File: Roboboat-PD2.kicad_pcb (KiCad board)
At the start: 2 copper layers, 78 x 60.7 mm, 52 parts, among them J1 14.4V, J10 Motor, J11 Motor, J12 Motor, J13 Motor, J14 Motor, J15 Motor, J16 Motor, J17 GND TP, J18 PGOOD TP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

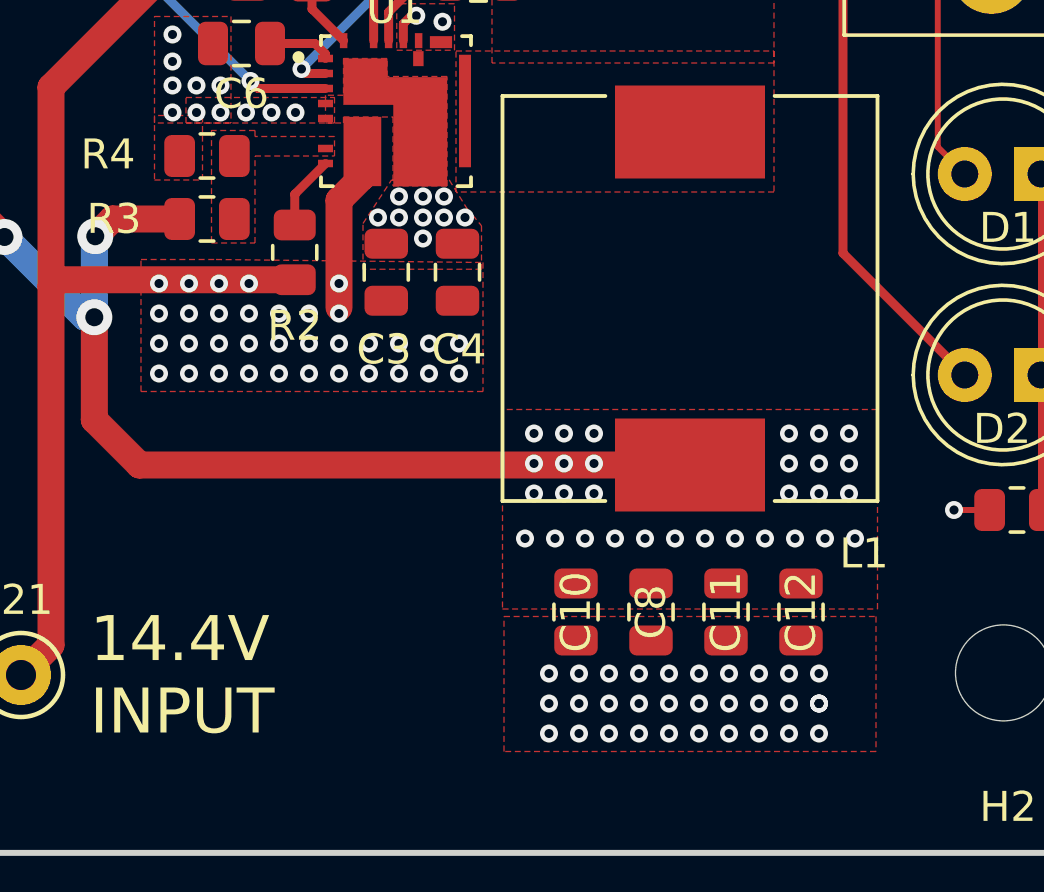
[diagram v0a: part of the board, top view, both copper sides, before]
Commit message: use less thermal vias
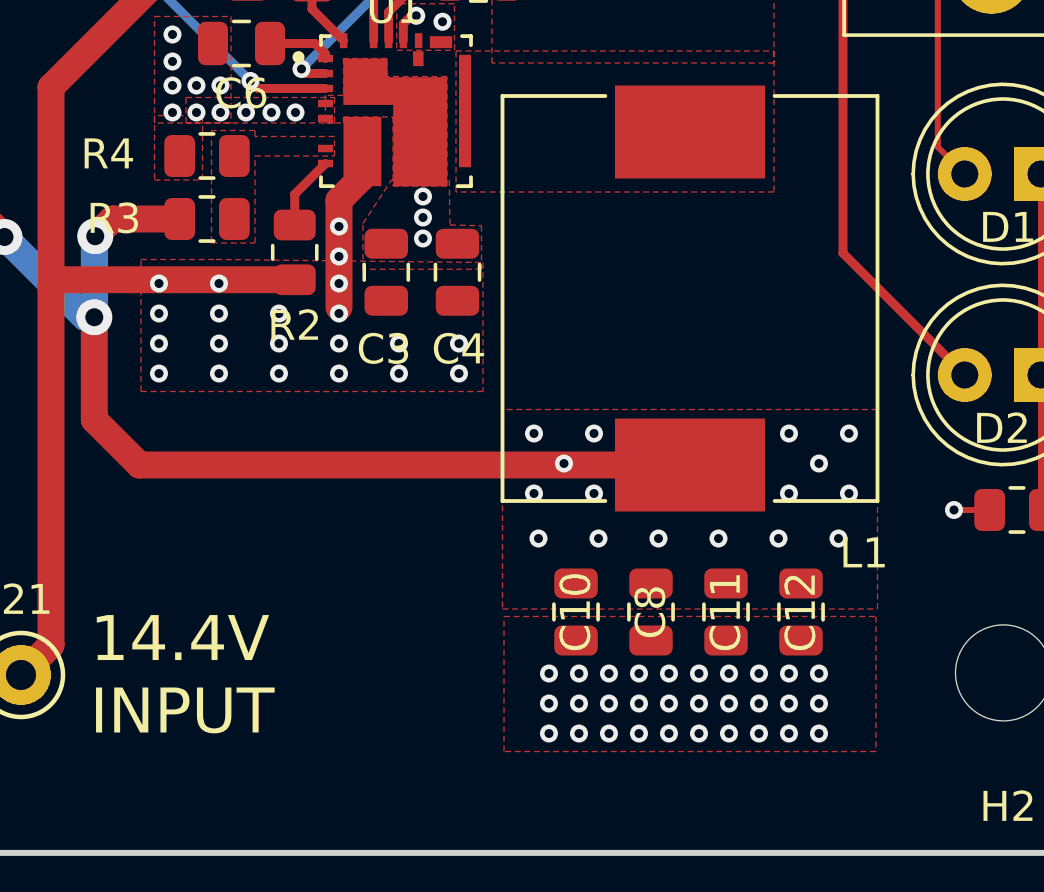
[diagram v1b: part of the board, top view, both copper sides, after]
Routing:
- net GND: vias 75 -> 68
- net +14.4V: vias 34 -> 21
- net +12V: vias 33 -> 19

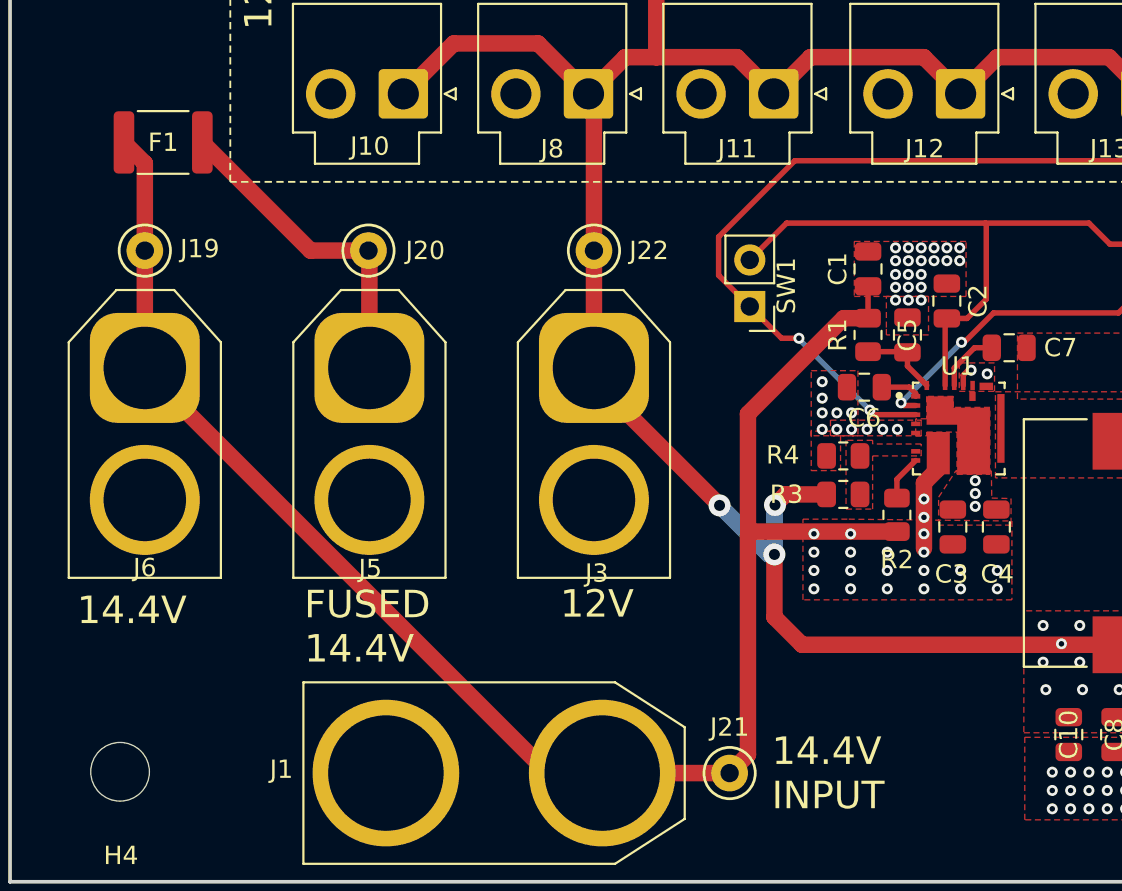
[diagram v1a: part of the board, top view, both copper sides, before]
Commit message: move fuse
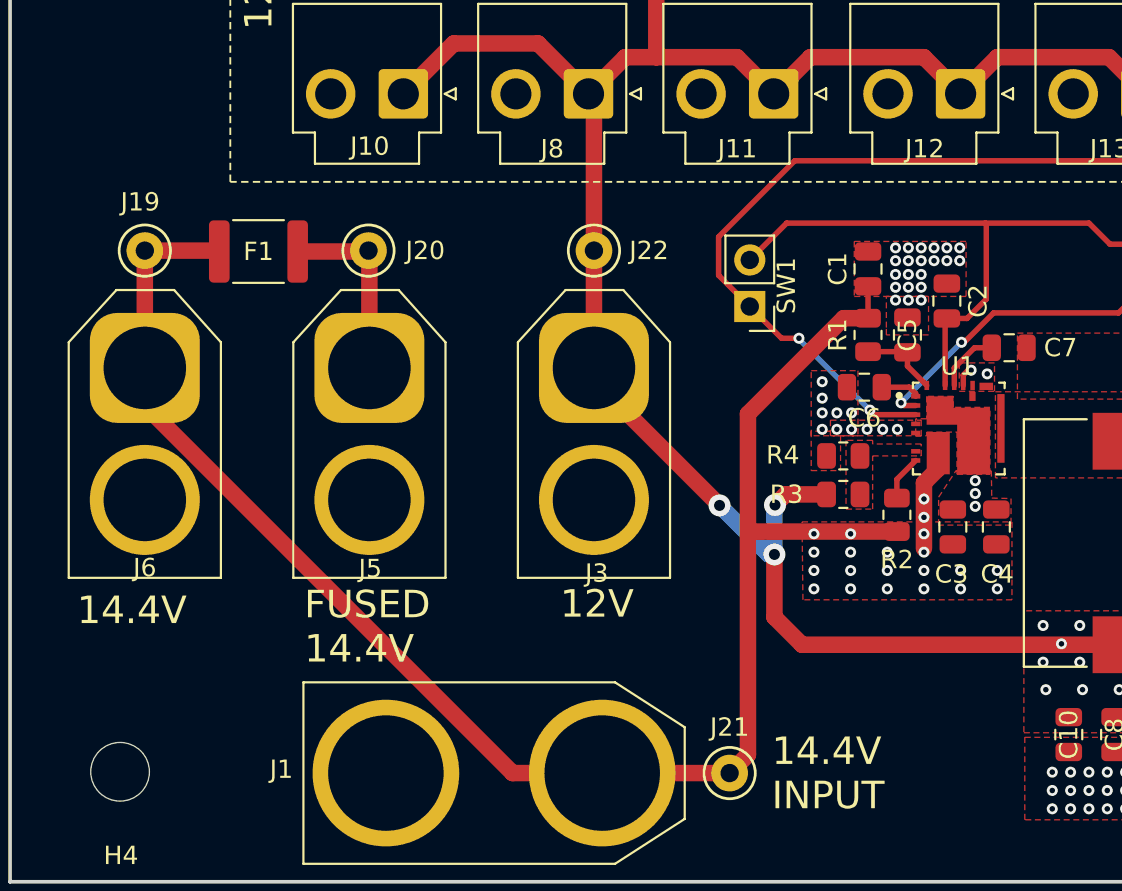
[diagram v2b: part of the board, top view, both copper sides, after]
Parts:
- moved F1 7.90 mm to (108.2, 94.6)
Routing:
- net /14.4_F: track 17.9 -> 10.2 mm
- net +14.4V: track 94.7 -> 96.6 mm
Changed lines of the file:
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@@
 		(tags "Through Hole Mount Test Points")
 		(property "Reference" "J19"
-			(at 3 -0.1 0)
+			(at -0.25 -2.65 0)
 			(layer "F.SilkS")
 			(effects
@@
 	(footprint "Fuse:Fuse_1812_4532Metric"
 		(layer "F.Cu")
-		(at 103 88.65 180)
+		(at 108.2 94.6 180)
 		(descr "Fuse SMD 1812 (4532 Metric), square (rectangular) end terminal, IPC_7351 nominal, (Body size source: https://www.nikhef.nl/pub/departments/mt/projects/detectorR_D/dtddice/ERJ2G.pdf), generated with kicad-footprint-generator")
 		(tags "fuse")
@@
 	)
 	(segment
-		(start 102 89.7875)
-		(end 100.8625 88.65)
+		(start 122.06188 123.05)
+		(end 126.95 123.05)
 		(width 0.9)
 		(layer "F.Cu")
@@
 	)
 	(segment
+		(start 102 102.98812)
+		(end 122.06188 123.05)
+		(width 0.9)
+		(layer "F.Cu")
+		(net 8)
+	)
+	(segment
 		(start 133.9 123.05)
 		(end 134.9 122.05)
@@
 	)
 	(segment
+		(start 102 94.55)
+		(end 106.0125 94.55)
+		(width 0.9)
+		(layer "F.Cu")
+		(net 8)
+	)
+	(segment
 		(start 145.28 106.445)
 		(end 145.28 105.6)
@@
 	)
 	(segment
-		(start 102 101.06188)
-		(end 123.98812 123.05)
+		(start 106.0125 94.55)
+		(end 106.0625 94.6)
 		(width 0.9)
 		(layer "F.Cu")
@@
 	)
 	(segment
-		(start 102 94.55)
-		(end 102 89.7875)
+		(start 102 100.95)
+		(end 102 102.98812)
 		(width 0.9)
 		(layer "F.Cu")
@@
 	)
 	(segment
-		(start 111.0375 94.55)
-		(end 105.1375 88.65)
+		(start 114.15 94.6)
+		(end 114.2 94.55)
 		(width 0.9)
 		(layer "F.Cu")
@@
 	)
 	(segment
-		(start 114.2 94.55)
-		(end 111.0375 94.55)
+		(start 110.3375 94.6)
+		(end 114.15 94.6)
 		(width 0.9)
 		(layer "F.Cu")
@@
 		(polygon
 			(pts
-				(xy 149.3 109.3) (xy 149.3 113.6) (xy 137.9 113.6) (xy 137.9 109.2) (xy 140.4 109.2)
+				(xy 149.3 109.35) (xy 149.3 113.6) (xy 137.9 113.6) (xy 137.85 109.35) (xy 140.4 109.35)
 			)
 		)

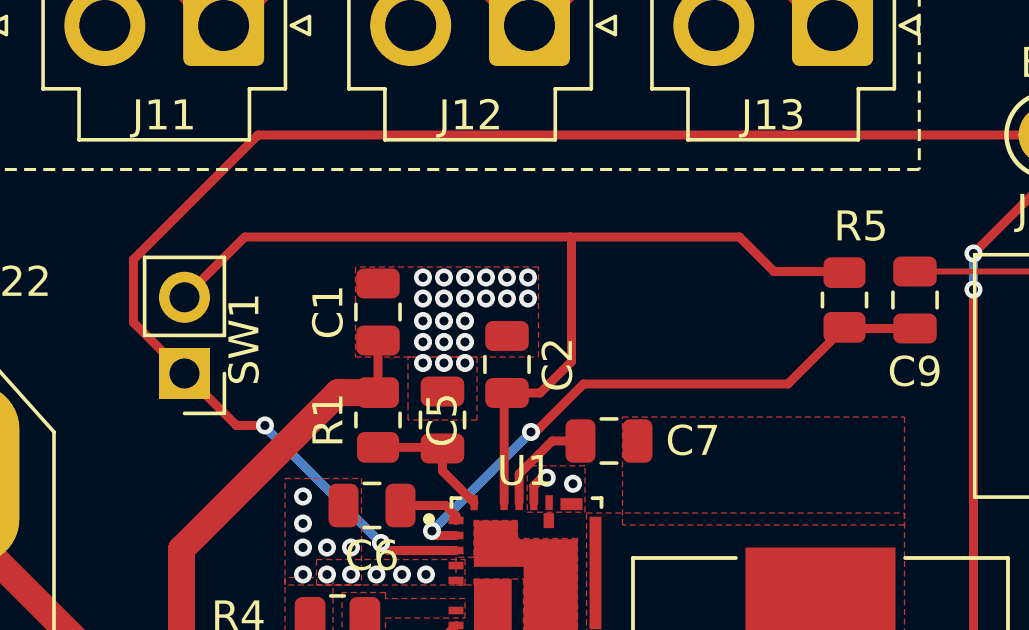
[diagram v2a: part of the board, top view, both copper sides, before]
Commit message: adjust VCC traces
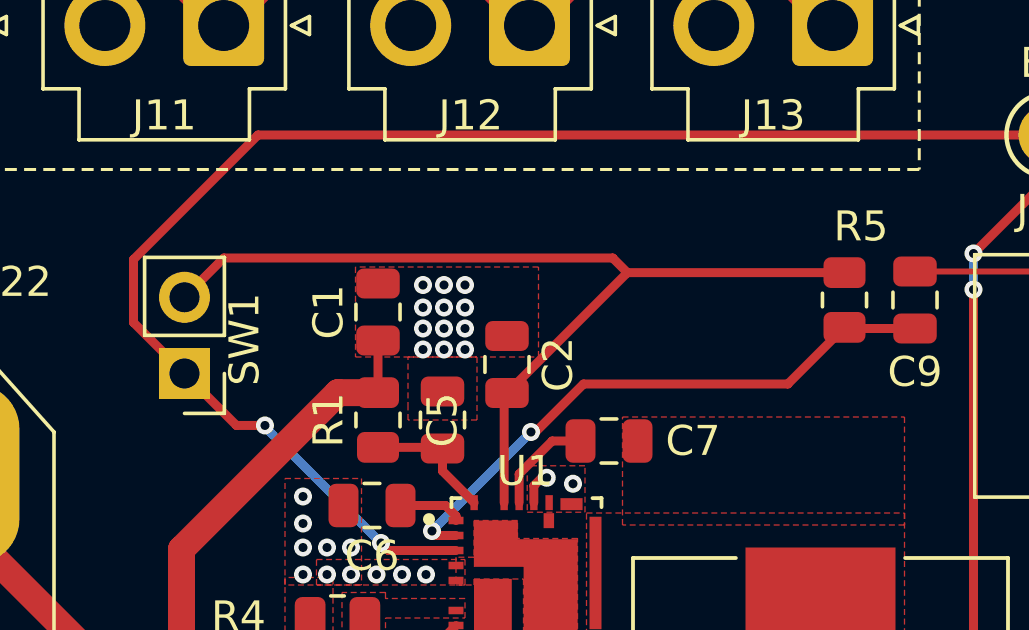
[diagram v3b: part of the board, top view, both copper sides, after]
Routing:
- net /VCC: track 33.6 -> 32.0 mm
- net GND: vias 68 -> 59
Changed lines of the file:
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@@
-	)
-	(via
-		(at 145.75 95.1)
-		(size 0.6)
-		(drill 0.3)
-		(layers "F.Cu" "B.Cu")
-		(free yes)
-		(net 1)
 	)
 	(via
@@
 	)
 	(via
-		(at 142.95 95.1)
-		(size 0.6)
-		(drill 0.3)
-		(layers "F.Cu" "B.Cu")
-		(free yes)
-		(net 1)
-	)
-	(via
-		(at 143.65 95.1)
-		(size 0.6)
-		(drill 0.3)
-		(layers "F.Cu" "B.Cu")
-		(free yes)
-		(net 1)
-	)
-	(via
-		(at 146.45 95.1)
+		(at 142.95 94.65)
+		(size 0.6)
+		(drill 0.3)
+		(layers "F.Cu" "B.Cu")
+		(free yes)
+		(net 1)
+	)
+	(via
+		(at 143.65 94.65)
 		(size 0.6)
 		(drill 0.3)
@@
 	)
 	(via
-		(at 142.95 95.85)
+		(at 142.95 95.4)
 		(size 0.6)
 		(drill 0.3)
@@
 	)
 	(via
-		(at 143.65 94.4)
-		(size 0.6)
-		(drill 0.3)
-		(layers "F.Cu" "B.Cu")
-		(free yes)
-		(net 1)
-	)
-	(via
 		(at 139.75 104.3)
 		(size 0.6)
@@
 	)
 	(via
-		(at 143.65 97.25)
+		(at 143.65 96.8)
 		(size 0.6)
 		(drill 0.3)
@@
 	)
 	(via
-		(at 144.35 95.1)
-		(size 0.6)
-		(drill 0.3)
-		(layers "F.Cu" "B.Cu")
-		(free yes)
-		(net 1)
-	)
-	(via
-		(at 143.65 95.85)
+		(at 144.35 94.65)
+		(size 0.6)
+		(drill 0.3)
+		(layers "F.Cu" "B.Cu")
+		(free yes)
+		(net 1)
+	)
+	(via
+		(at 143.65 95.4)
 		(size 0.6)
 		(drill 0.3)
@@
 	)
 	(via
-		(at 144.35 94.4)
-		(size 0.6)
-		(drill 0.3)
-		(layers "F.Cu" "B.Cu")
-		(free yes)
-		(net 1)
-	)
-	(via
 		(at 153.5 125)
 		(size 0.6)
@@
 	)
 	(via
-		(at 145.75 94.4)
-		(size 0.6)
-		(drill 0.3)
-		(layers "F.Cu" "B.Cu")
-		(free yes)
-		(net 1)
-	)
-	(via
 		(at 151.5 123)
 		(size 0.6)
@@
 	)
 	(via
-		(at 146.45 94.4)
-		(size 0.6)
-		(drill 0.3)
-		(layers "F.Cu" "B.Cu")
-		(free yes)
-		(net 1)
-	)
-	(via
 		(at 153.5 124)
 		(size 0.6)
@@
 	)
 	(via
-		(at 142.95 97.25)
-		(size 0.6)
-		(drill 0.3)
-		(layers "F.Cu" "B.Cu")
-		(free yes)
-		(net 1)
-	)
-	(via
-		(at 142.95 96.55)
+		(at 142.95 96.8)
+		(size 0.6)
+		(drill 0.3)
+		(layers "F.Cu" "B.Cu")
+		(free yes)
+		(net 1)
+	)
+	(via
+		(at 142.95 96.1)
 		(size 0.6)
 		(drill 0.3)
@@
 	)
 	(via
-		(at 145.05 95.1)
-		(size 0.6)
-		(drill 0.3)
-		(layers "F.Cu" "B.Cu")
-		(free yes)
-		(net 1)
-	)
-	(via
-		(at 144.35 95.85)
+		(at 144.35 95.4)
 		(size 0.6)
 		(drill 0.3)
@@
 	)
 	(via
-		(at 145.05 94.4)
-		(size 0.6)
-		(drill 0.3)
-		(layers "F.Cu" "B.Cu")
-		(free yes)
-		(net 1)
-	)
-	(via
 		(at 140.55 104.3)
 		(size 0.6)
@@
 	)
 	(via
-		(at 142.95 94.4)
-		(size 0.6)
-		(drill 0.3)
-		(layers "F.Cu" "B.Cu")
-		(free yes)
-		(net 1)
-	)
-	(via
 		(at 157.5 125)
 		(size 0.6)
@@
 	)
 	(via
-		(at 144.35 97.25)
+		(at 144.35 96.8)
 		(size 0.6)
 		(drill 0.3)
@@
 	)
 	(via
-		(at 143.65 96.55)
+		(at 143.65 96.1)
 		(size 0.6)
 		(drill 0.3)
@@
 	)
 	(via
-		(at 144.35 96.55)
+		(at 144.35 96.1)
 		(size 0.6)
 		(drill 0.3)
@@
 	)
 	(segment
-		(start 147.85 93.05)
-		(end 153.5 93.05)
+		(start 157 94.2375)
+		(end 149.7625 94.2375)
 		(width 0.3)
 		(layer "F.Cu")
@@
 	)
 	(segment
-		(start 137.01 93.05)
-		(end 147.85 93.05)
+		(start 149.275 93.75)
+		(end 149.7625 94.2375)
 		(width 0.3)
 		(layer "F.Cu")
@@
 	)
 	(segment
-		(start 147.9 93.1)
-		(end 147.85 93.05)
+		(start 135 95.06)
+		(end 136.31 93.75)
 		(width 0.3)
 		(layer "F.Cu")
@@
 	)
 	(segment
-		(start 147.9 97.2)
-		(end 147.9 93.1)
+		(start 136.31 93.75)
+		(end 149.275 93.75)
 		(width 0.3)
 		(layer "F.Cu")
@@
 	)
 	(segment
-		(start 153.5 93.05)
-		(end 154.65 94.2)
-		(width 0.3)
-		(layer "F.Cu")
-		(net 11)
-	)
-	(segment
-		(start 145.75 98.25)
-		(end 146.85 98.25)
-		(width 0.3)
-		(layer "F.Cu")
-		(net 11)
-	)
-	(segment
-		(start 135 95.06)
-		(end 137.01 93.05)
-		(width 0.3)
-		(layer "F.Cu")
-		(net 11)
-	)
-	(segment
-		(start 146.85 98.25)
-		(end 147.9 97.2)
-		(width 0.3)
-		(layer "F.Cu")
-		(net 11)
-	)
-	(segment
-		(start 154.65 94.2)
-		(end 156.9625 94.2)
-		(width 0.3)
-		(layer "F.Cu")
+		(start 149.7625 94.2375)
+		(end 145.75 98.25)
+		(width 0.3)
+		(layer "F.Cu")

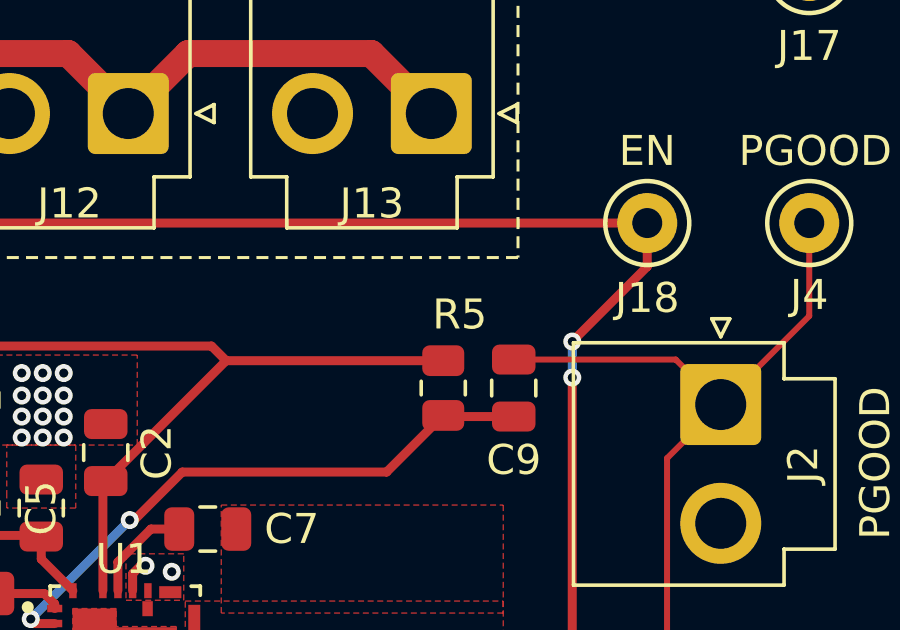
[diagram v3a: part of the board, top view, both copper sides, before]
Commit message: fix R_TON value
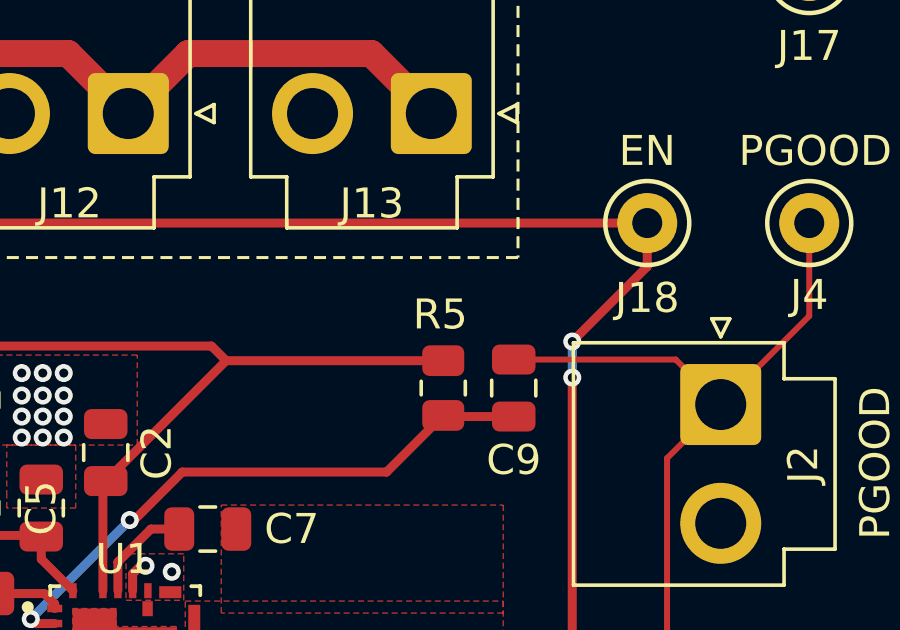
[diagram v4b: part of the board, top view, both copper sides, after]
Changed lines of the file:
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@@
 		(tags "resistor")
 		(property "Reference" "R5"
-			(at -2.45 -0.55 0)
+			(at -2.45 0.1 0)
 			(layer "F.SilkS")
 			(effects
